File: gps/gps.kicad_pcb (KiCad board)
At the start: 2 copper layers, 38 x 38 mm, 66 parts, among them P1 PWR, P2 CTL, P3 UART, U1 USB_A_FEMALE, U2 TXS0102, U3 SE880, U4 ABS25, U5 SGP25C, U6 KT2520, U7 TPS76333, U8 TPS76318

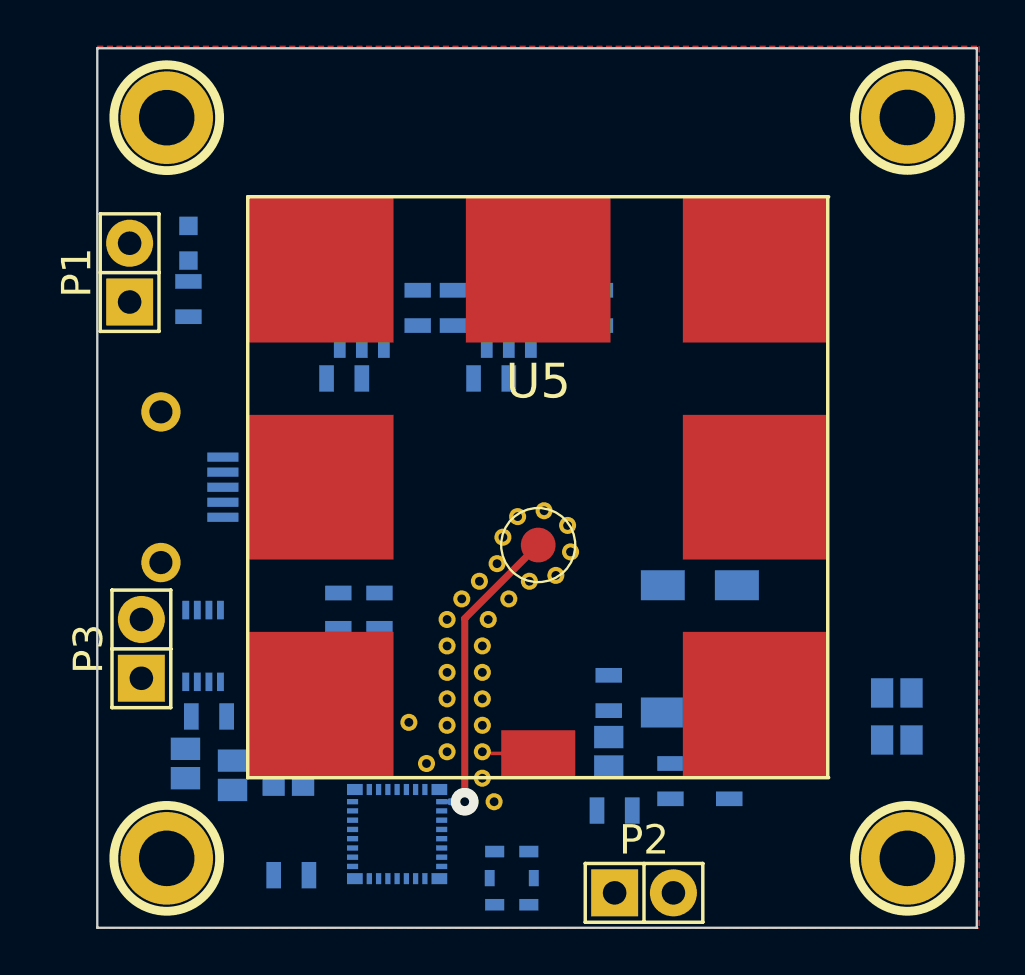
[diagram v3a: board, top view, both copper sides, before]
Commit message: finished routing. need to add stitching vias
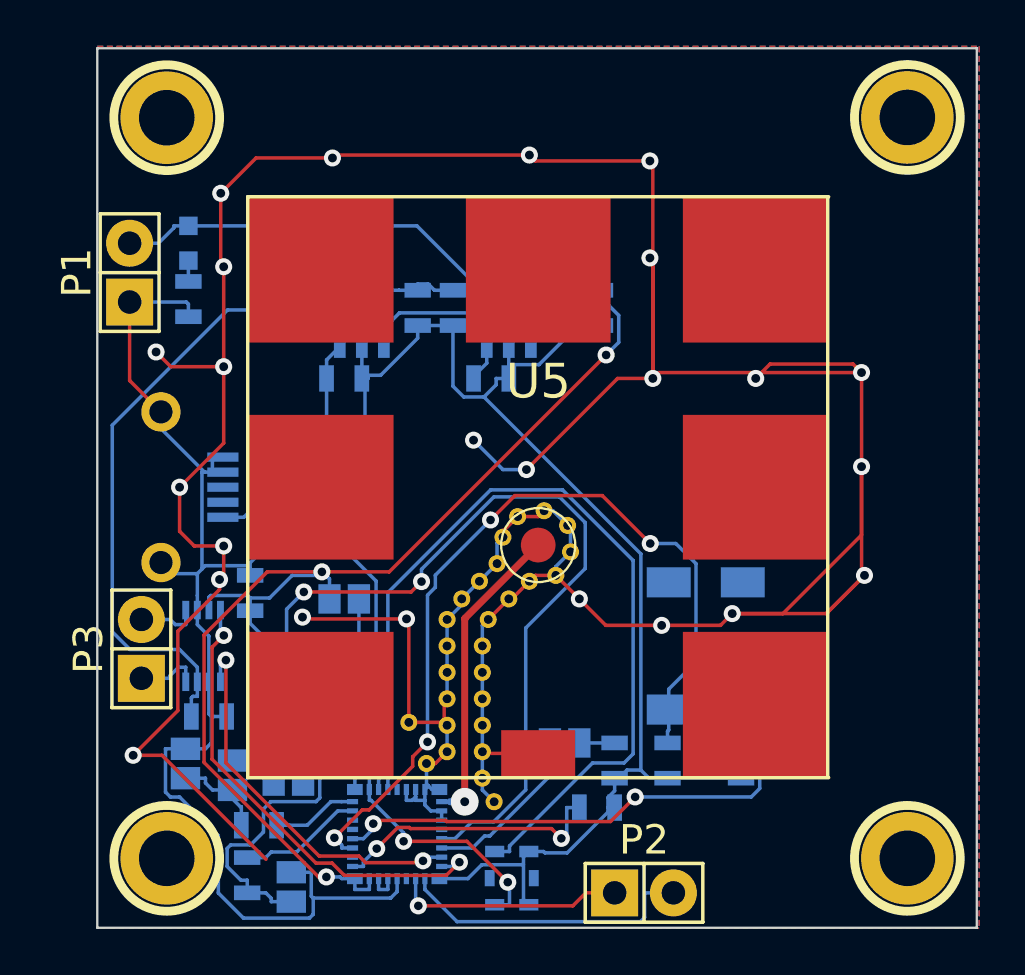
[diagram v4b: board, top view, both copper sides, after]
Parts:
- moved JP6 26.9 mm to (160.8, 68.1), turned to 0 degrees
- moved JP5 24.2 mm to (163.1, 55.6), turned to 90 degrees
- moved R6 12.8 mm to (158.9, 67.6), turned to 90 degrees
- moved C1 12.3 mm to (159.0, 55.4), turned to 90 degrees
- moved R5 9.88 mm to (159.4, 65.4), turned to 0 degrees
- moved R3 2.93 mm to (174.8, 62.6), turned to 270 degrees
- moved JP1 1.94 mm to (172.6, 61.8), turned to 90 degrees
- moved C4 1.02 mm to (180.2, 62.6)
- moved C2 0.90 mm to (177.0, 62.6)
- moved R2 0.77 mm to (174.0, 64.6)
- moved U4 0.28 mm to (178.7, 57.7)
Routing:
- net AGND: track 2.44 -> 181.2 mm, vias 0 -> 24
- net DGND: track 0.00 -> 134.8 mm
- net 1.8V: track 0.00 -> 61.8 mm, vias 0 -> 3
- net 5V: track 0.00 -> 40.8 mm
- net Net-(JP2-Pad2): track 0.00 -> 40.5 mm, vias 0 -> 2
- net Net-(U3-Pad21): track 0.00 -> 38.4 mm
- net Net-(C2-Pad1): track 0.00 -> 36.5 mm, vias 0 -> 4
- net 3.3V: track 0.00 -> 33.1 mm
- net Net-(C4-Pad1): track 0.00 -> 22.7 mm, vias 0 -> 2
- net Net-(U2-Pad4): track 0.00 -> 20.6 mm, vias 0 -> 2
- net Net-(JP5-Pad1): track 0.00 -> 19.4 mm
- net Net-(U2-Pad5): track 0.00 -> 16.7 mm, vias 0 -> 2
- net SYSTEM_ON: track 0.00 -> 12.9 mm
- net Net-(R2-Pad2): track 0.00 -> 12.0 mm, vias 0 -> 2
- net Net-(C5-Pad1): track 0.00 -> 11.2 mm, vias 0 -> 2
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- added copper zone on B.Cu, net AGND
- added copper zone on F.Cu, net AGND
- removed copper zone on F.Cu, net (none)

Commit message: Finished the GPS module
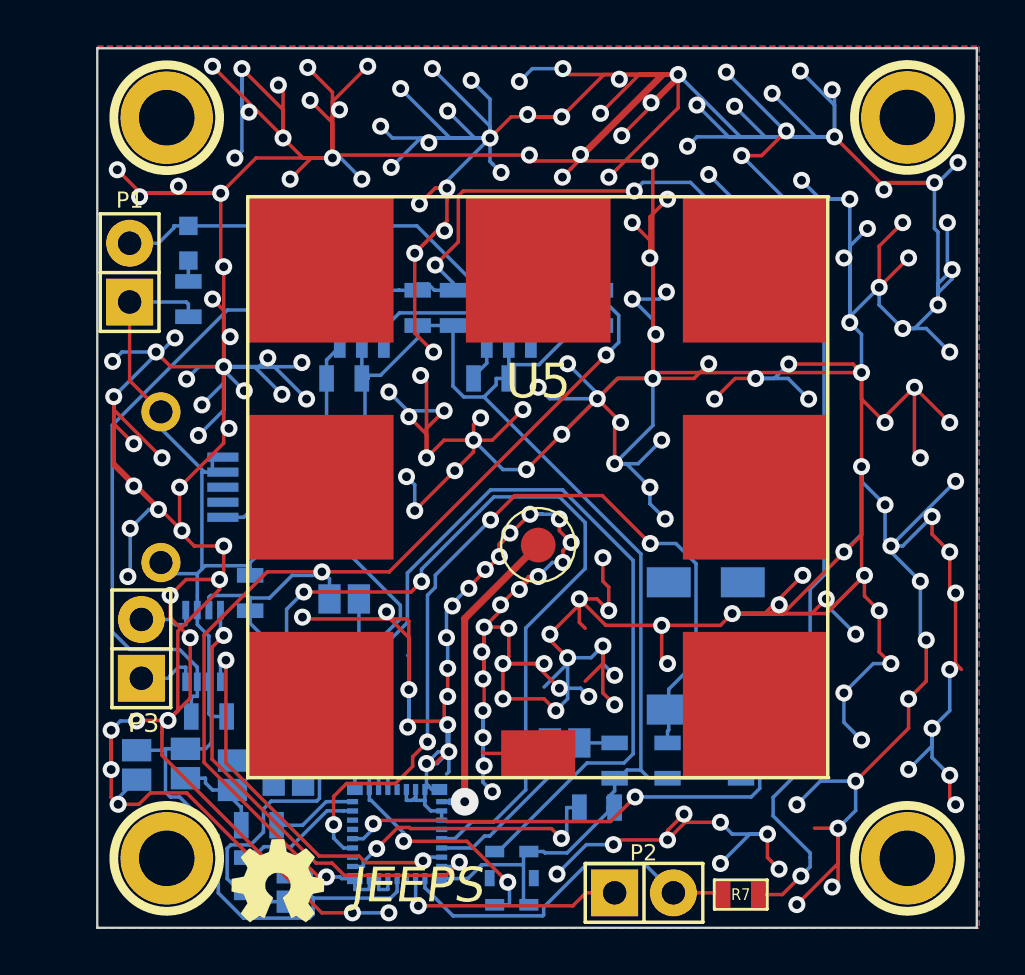
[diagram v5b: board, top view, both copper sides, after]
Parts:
- removed ant_via, ant_via1, ant_via10, ant_via11, ant_via12, ant_via14, ant_via15, ant_via16, ant_via17, ant_via18, ant_via19, ant_via2, ant_via20, ant_via21, ant_via22, ant_via23, ant_via24, ant_via25, ant_via26, ant_via27, ant_via28, ant_via3, ant_via4, ant_via5, ant_via7, ant_via8, ant_via9: VAL**, gps:ant_via
- added G***: LOGO, usb_hub:oshw, F.Cu at (160.2, 67.8)
- added G***: LOGO, usb_hub:LOGO, B.Cu at (171.2, 38.8)
- added JP7: JUMPER, Connect:GS2, B.Cu at (154.1, 62.8)
- added R7: 10k, SMD_Packages:SMD-0603, F.Cu at (180.2, 68.4)
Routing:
- net AGND: track 181.2 -> 723.2 mm, vias 24 -> 223
- net 3.3V: track 33.1 -> 84.4 mm, vias 0 -> 3
- net (no net): track 0.00 -> 15.9 mm, vias 0 -> 8
- net SYSTEM_ON: track 12.9 -> 15.4 mm
- net DGND: track 134.8 -> 137.1 mm
- net Net-(C2-Pad1): track 36.5 -> 37.6 mm
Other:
- board text added: "JEEPS"

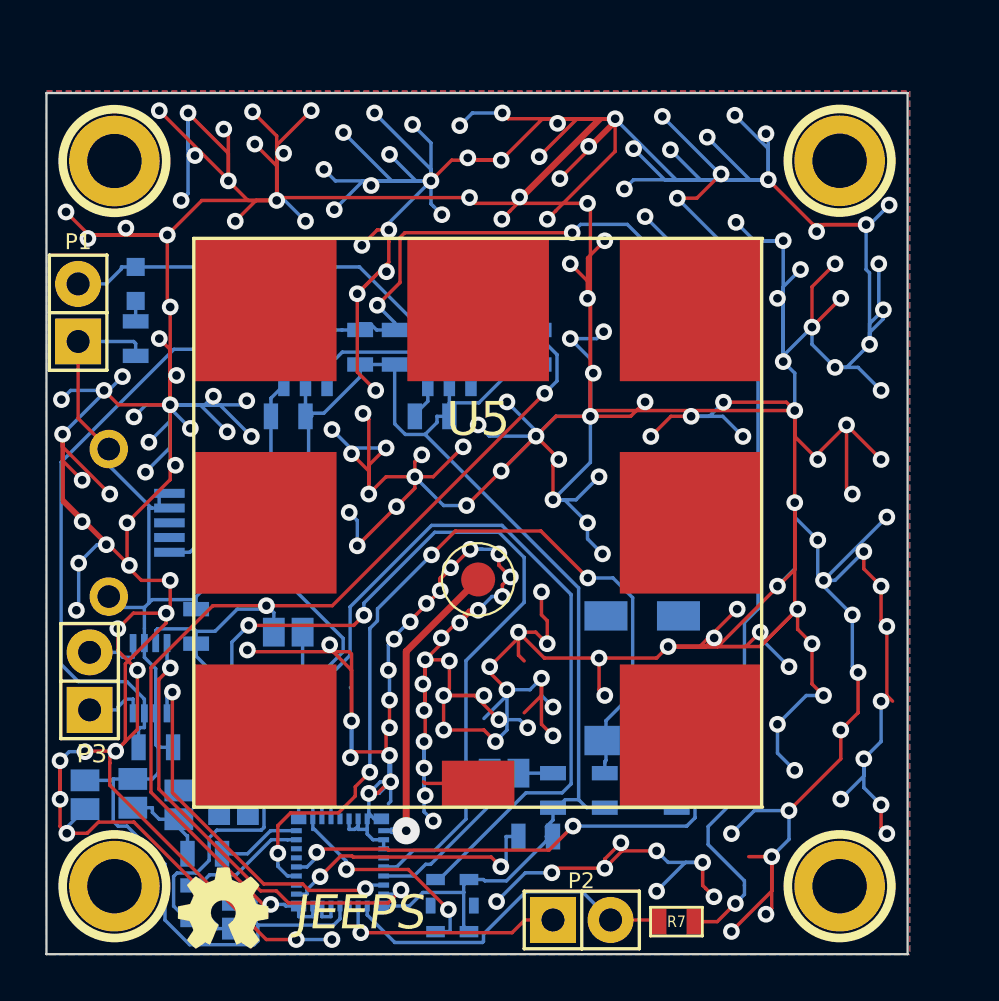
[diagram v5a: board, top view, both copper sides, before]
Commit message: sent usb_hub for review. Finished gps schematic/bom.
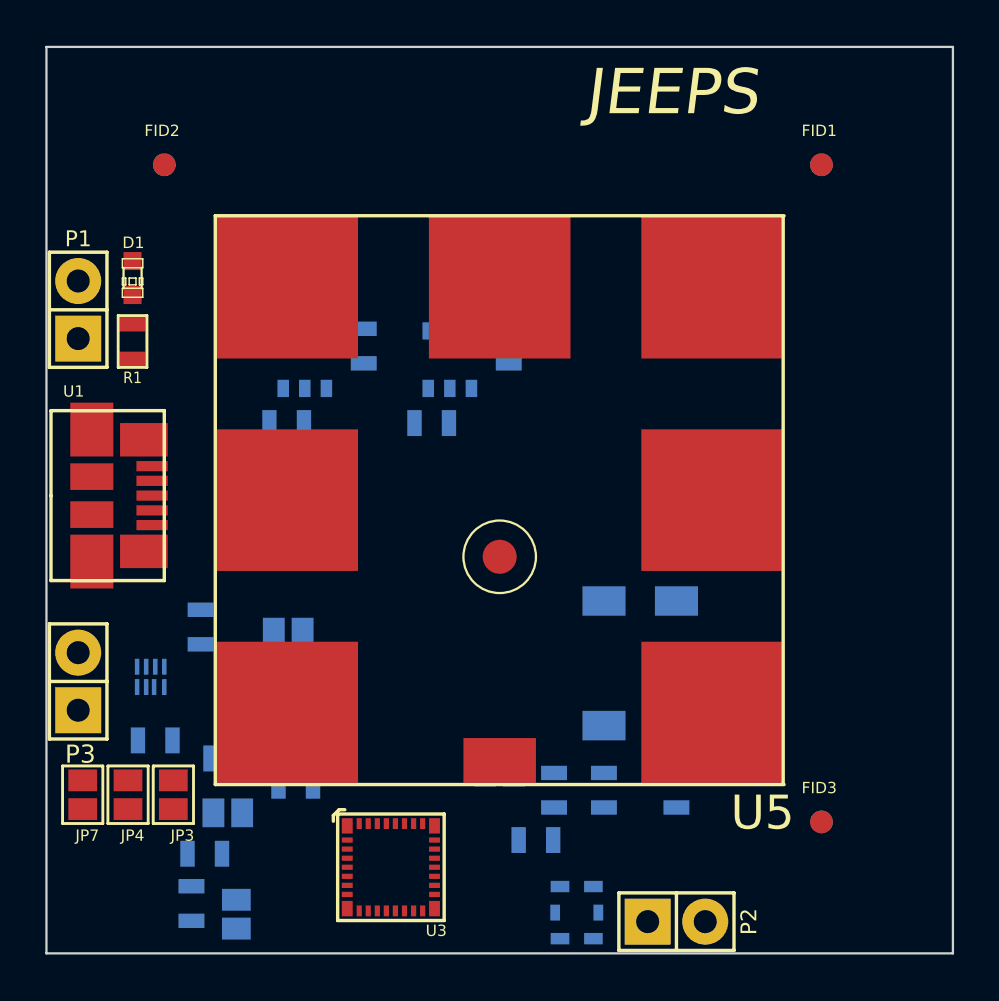
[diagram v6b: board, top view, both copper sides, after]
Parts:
- removed 1PIN, 2PIN, 3PIN, 4PIN: P***, Connect:1pin
- removed C10, C11: .1uF, SMD_Packages:SMD-0603
- removed G***: LOGO, usb_hub:oshw
- removed G***: LOGO, usb_hub:LOGO
- removed R7: 10k, SMD_Packages:SMD-0603
- added FID1: VAL**, apro_lib:SBA_FID, F.Cu at (186.6, 35.0)
- added FID2: VAL**, apro_lib:SBA_FID, F.Cu at (157.6, 35.0)
- added FID3: VAL**, apro_lib:SBA_FID, F.Cu at (186.6, 64.0)
- added FID4: VAL**, apro_lib:SBA_FID, B.Cu at (186.6, 35.0)
- added FID5: VAL**, apro_lib:SBA_FID, B.Cu at (157.6, 35.0)
- added FID6: VAL**, apro_lib:SBA_FID, B.Cu at (186.6, 64.0)
- D1: value LED(G) -> LED; moved to F.Cu
- JP3, JP4, JP7, U3: moved to F.Cu
- R1: value 510 -> 1k; moved to F.Cu
- U1: footprint ab2_usb:AB2_USB_MICRO_SMD -> apro_lib:MICRO_USB; moved to F.Cu
- moved U6 5.50 mm to (175.8, 68.0), turned to 270 degrees
- moved P2 4.18 mm to (180.2, 68.4)
- moved U1 2.33 mm to (154.4, 49.6), turned to 0 degrees
- moved U3 2.26 mm to (167.6, 66.0), turned to 0 degrees
- moved U5 1.38 mm to (172.4, 49.8)
- moved U4 0.66 mm to (178.6, 57.0)
- moved JP3 0.51 mm to (158.0, 62.8), turned to 180 degrees
- moved P3 0.51 mm to (153.8, 57.8)
- moved R4 0.47 mm to (160.4, 61.2)
- moved C3 0.31 mm to (157.2, 60.4)
- moved C6 0.31 mm to (163.0, 46.4)
- moved C7 0.30 mm to (169.4, 46.4)
- moved D1 0.29 mm to (156.2, 40.0)
- moved JP2 0.27 mm to (160.4, 63.6)
- moved JP4 0.22 mm to (156.0, 62.8), turned to 180 degrees
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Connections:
- R2 pad 1: DGND -> Net-(R2-Pad1)
- R2 pad 2: Net-(R2-Pad2) -> DGND
- U3 pad 10: Net-(R2-Pad2) -> Net-(R2-Pad1)
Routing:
- net AGND: track 723.2 -> 0.00 mm, vias 223 -> 0
- net DGND: track 137.1 -> 0.00 mm
- net 3.3V: track 84.4 -> 0.00 mm, vias 3 -> 0
- net 1.8V: track 61.8 -> 0.00 mm, vias 3 -> 0
- net 5V: track 40.8 -> 0.00 mm
- net Net-(JP2-Pad2): track 40.5 -> 0.00 mm, vias 2 -> 0
- net Net-(U3-Pad21): track 38.3 -> 0.00 mm
- net Net-(C2-Pad1): track 37.6 -> 0.00 mm, vias 4 -> 0
- net Net-(C4-Pad1): track 22.7 -> 0.00 mm, vias 2 -> 0
- net Net-(U2-Pad4): track 20.6 -> 0.00 mm, vias 2 -> 0
- net Net-(JP5-Pad1): track 19.4 -> 0.00 mm
- net Net-(U2-Pad5): track 16.7 -> 0.00 mm, vias 2 -> 0
- net (no net): track 15.9 -> 0.00 mm, vias 8 -> 0
- net SYSTEM_ON: track 15.4 -> 0.00 mm
- net /50ohm: track 13.4 -> 0.00 mm, vias 1 -> 0
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- removed copper zone on B.Cu, net AGND
- removed copper zone on F.Cu, net AGND
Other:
- board size 38 x 38 mm -> 40 x 40 mm
- net class Default: via_dia 0.7366 -> 0.6858; via_drill 0.381 -> 0.3302
- net class ohm: via_drill 0.381 -> 0.3302
- rule via_min_drill: 0.381 -> 0.3302
- rule via_min_size: 0.7366 -> 0.6858

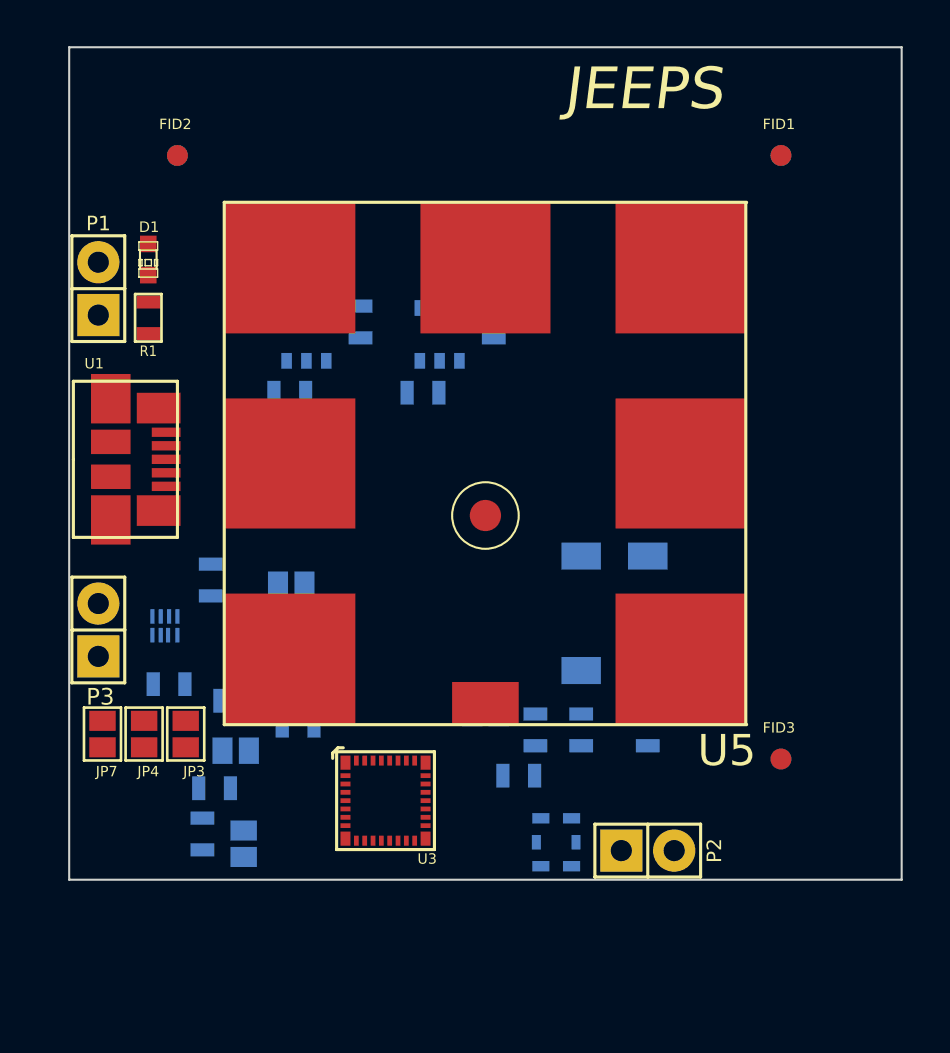
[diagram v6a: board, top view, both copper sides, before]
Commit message: Need to route the 50ohm trace
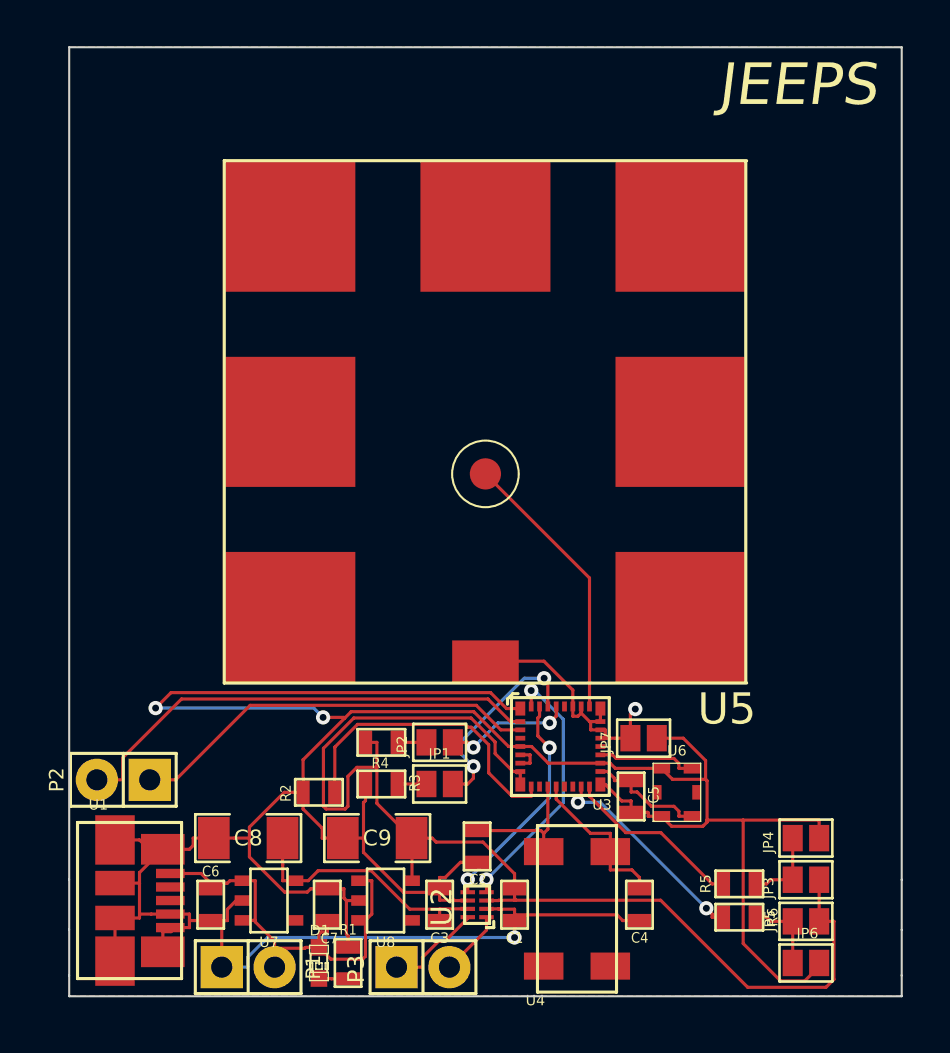
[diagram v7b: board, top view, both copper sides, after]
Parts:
- removed FID1, FID2, FID3, FID4, FID5, FID6: VAL**, apro_lib:SBA_FID
- C1, C2, C3, C4, C5, C6, C7, JP1, JP2, JP5, JP6, R2, R3, R4, R5, R6, U2, U4, U6, U7, U8: moved to F.Cu
- C8, C9: footprint SMD_Packages:SMD-0603 -> SMD_Packages:SMD-1206; moved to F.Cu
- moved D1 34.8 mm to (164.4, 73.8)
- moved P1 33.4 mm to (161.0, 74.0), turned to 0 degrees
- moved R1 32.5 mm to (165.8, 73.8), turned to 90 degrees
- moved JP4 32.2 mm to (187.8, 67.8), turned to 90 degrees
- moved JP3 30.6 mm to (187.8, 69.8), turned to 90 degrees
- moved JP5 29.6 mm to (187.8, 71.8)
- moved JP6 27.6 mm to (187.8, 73.8), turned to 90 degrees
- moved U8 27.3 mm to (167.6, 70.8), turned to 270 degrees
- moved U7 27.3 mm to (162.0, 70.8), turned to 270 degrees
- moved R6 26.1 mm to (184.6, 71.6), turned to 180 degrees
- moved JP7 26.0 mm to (180.0, 63.0), turned to 90 degrees
- moved R5 25.6 mm to (184.6, 70.0), turned to 180 degrees
- moved P2 25.4 mm to (155.0, 65.0), turned to 180 degrees
- moved C9 25.4 mm to (167.2, 67.8), turned to 180 degrees
- moved C8 25.4 mm to (161.0, 67.8), turned to 180 degrees
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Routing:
- net DGND: track 0.00 -> 160.2 mm, vias 0 -> 3
- net 1.8V: track 0.00 -> 58.4 mm
- net SYSTEM_ON: track 0.00 -> 23.0 mm
- net 5V: track 0.00 -> 20.7 mm
- net ON_OFF: track 0.00 -> 19.8 mm
- net Net-(R2-Pad1): track 0.00 -> 14.8 mm
- net /50ohm: track 0.00 -> 13.2 mm
- net AGND: track 0.00 -> 13.0 mm, vias 0 -> 1
- net Net-(U2-Pad4): track 0.00 -> 12.7 mm, vias 0 -> 2
- net 3.3V: track 0.00 -> 12.5 mm
- net Net-(U2-Pad5): track 0.00 -> 10.8 mm, vias 0 -> 2
- net Net-(R6-Pad2): track 0.00 -> 10.2 mm, vias 0 -> 2
- net Net-(JP1-Pad2): track 0.00 -> 9.78 mm, vias 0 -> 2
- net Net-(R5-Pad2): track 0.00 -> 8.65 mm
- net Net-(C4-Pad1): track 0.00 -> 7.74 mm
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- added copper zone on B.Cu, net AGND
- added copper zone on F.Cu, net AGND
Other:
- board size 40 x 40 mm -> 40 x 45.6 mm
